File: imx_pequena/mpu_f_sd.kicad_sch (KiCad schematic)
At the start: 13 parts, among them J2 Micro_SD_Card, U1 MCIMX6Z0DVM09AB

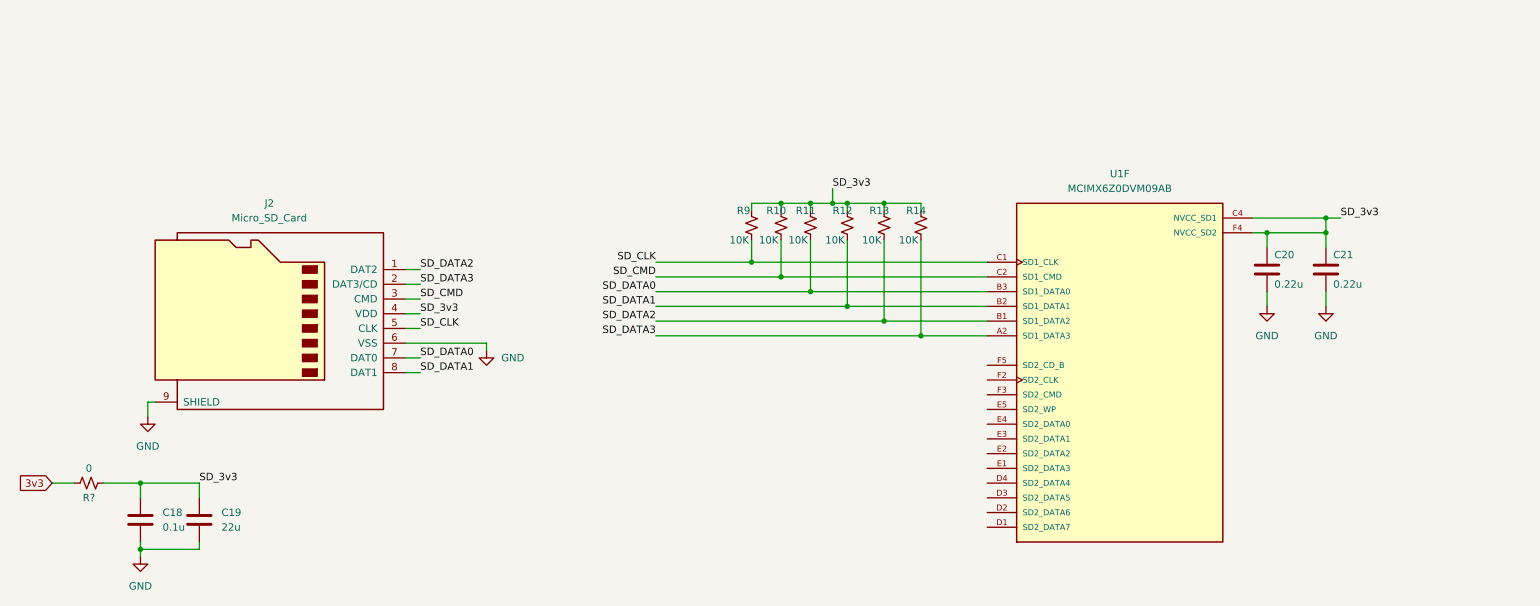
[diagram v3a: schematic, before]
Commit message: Updated pin mappings
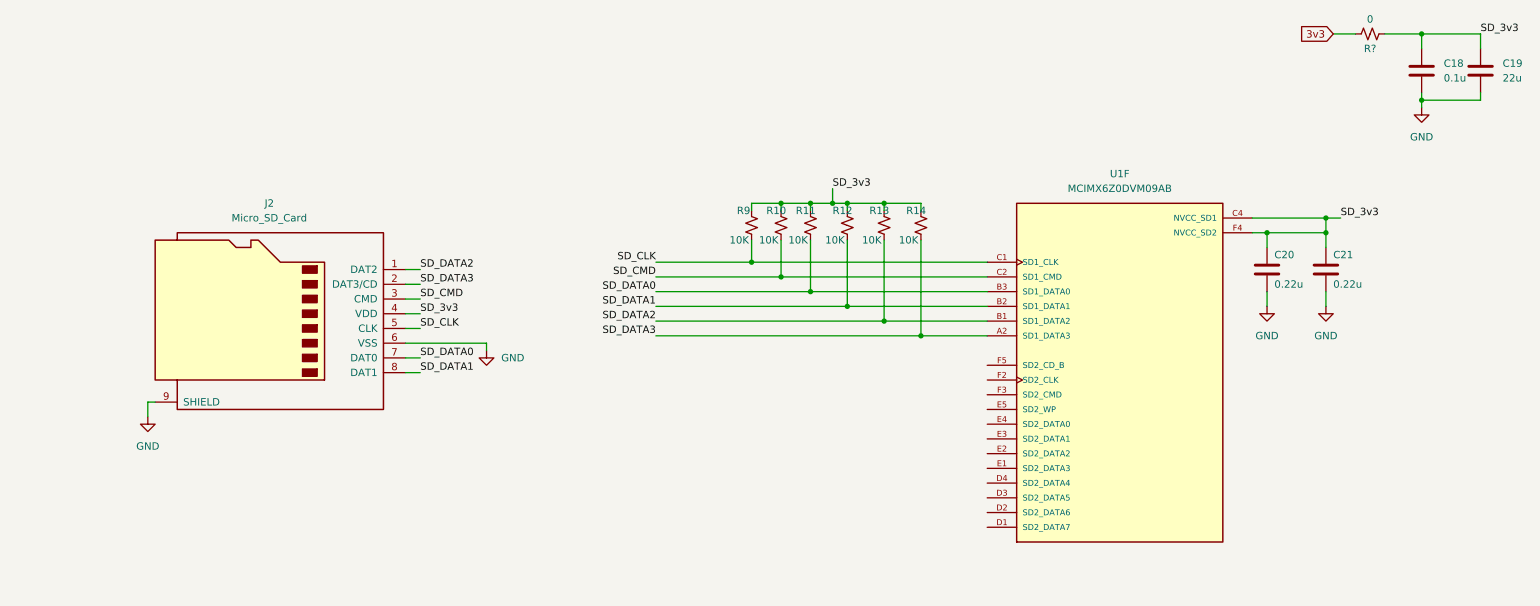
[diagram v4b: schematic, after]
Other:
- moved on the sheet: C18, C19, R?
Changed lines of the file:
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@@
   (junction (at 151.13 50.8) (diameter 0) (color 0 0 0 0)
   )
-  (junction (at 40.64 99.06) (diameter 0) (color 0 0 0 0)
+  (junction (at 261.62 21.59) (diameter 0) (color 0 0 0 0)
   )
   (junction (at 146.05 60.96) (diameter 0) (color 0 0 0 0)
@@
   (junction (at 156.21 50.8) (diameter 0) (color 0 0 0 0)
   )
-  (junction (at 40.64 110.49) (diameter 0) (color 0 0 0 0)
+  (junction (at 261.62 33.02) (diameter 0) (color 0 0 0 0)
   )
   (junction (at 160.02 50.8) (diameter 0) (color 0 0 0 0)
@@
     (stroke (width 0) (type default) (color 0 0 0 0))
   )
-  (wire (pts (xy 40.64 110.49) (xy 50.8 110.49))
+  (wire (pts (xy 261.62 33.02) (xy 271.78 33.02))
     (stroke (width 0) (type default) (color 0 0 0 0))
   )
@@
     (stroke (width 0) (type default) (color 0 0 0 0))
   )
-  (wire (pts (xy 40.64 109.22) (xy 40.64 110.49))
+  (wire (pts (xy 261.62 31.75) (xy 261.62 33.02))
     (stroke (width 0) (type default) (color 0 0 0 0))
   )
@@
     (stroke (width 0) (type default) (color 0 0 0 0))
   )
-  (wire (pts (xy 34.29 99.06) (xy 40.64 99.06))
+  (wire (pts (xy 255.27 21.59) (xy 261.62 21.59))
     (stroke (width 0) (type default) (color 0 0 0 0))
   )
@@
     (stroke (width 0) (type default) (color 0 0 0 0))
   )
-  (wire (pts (xy 50.8 99.06) (xy 50.8 101.6))
+  (wire (pts (xy 271.78 21.59) (xy 271.78 24.13))
     (stroke (width 0) (type default) (color 0 0 0 0))
   )
@@
     (stroke (width 0) (type default) (color 0 0 0 0))
   )
-  (wire (pts (xy 40.64 110.49) (xy 40.64 111.76))
+  (wire (pts (xy 261.62 33.02) (xy 261.62 34.29))
     (stroke (width 0) (type default) (color 0 0 0 0))
   )
@@
     (stroke (width 0) (type default) (color 0 0 0 0))
   )
-  (wire (pts (xy 50.8 110.49) (xy 50.8 109.22))
+  (wire (pts (xy 271.78 33.02) (xy 271.78 31.75))
     (stroke (width 0) (type default) (color 0 0 0 0))
   )
@@
     (stroke (width 0) (type default) (color 0 0 0 0))
   )
-  (wire (pts (xy 40.64 99.06) (xy 50.8 99.06))
+  (wire (pts (xy 261.62 21.59) (xy 271.78 21.59))
     (stroke (width 0) (type default) (color 0 0 0 0))
   )
@@
     (stroke (width 0) (type default) (color 0 0 0 0))
   )
-  (wire (pts (xy 29.21 99.06) (xy 25.4 99.06))
+  (wire (pts (xy 250.19 21.59) (xy 246.38 21.59))
     (stroke (width 0) (type default) (color 0 0 0 0))
   )
@@
     (stroke (width 0) (type default) (color 0 0 0 0))
   )
-  (wire (pts (xy 40.64 99.06) (xy 40.64 101.6))
+  (wire (pts (xy 261.62 21.59) (xy 261.62 24.13))
     (stroke (width 0) (type default) (color 0 0 0 0))
   )
@@
     (effects (font (size 1.27 1.27)) (justify left bottom))
   )
-  (label "SD_3v3" (at 50.8 99.06 0)
+  (label "SD_3v3" (at 271.78 21.59 0)
     (effects (font (size 1.27 1.27)) (justify left bottom))
   )
@@
     (effects (font (size 1.27 1.27)) (justify left bottom))
   )
-  (global_label "3v3" (shape input) (at 25.4 99.06 180) (fields_autoplaced)
+  (global_label "3v3" (shape input) (at 246.38 21.59 180) (fields_autoplaced)
     (effects (font (size 1.27 1.27)) (justify right))
-    (property "Intersheet References" "${INTERSHEET_REFS}" (id 0) (at 19.6002 99.1394 0)
+    (property "Intersheet References" "${INTERSHEET_REFS}" (id 0) (at 240.5802 21.6694 0)
       (effects (font (size 1.27 1.27)) (justify right) hide)
     )
@@
     (pin "1")
   )
-  (symbol (lib_id "Device:C") (at 50.8 105.41 0) (unit 1)
-    (in_bom yes) (on_board yes) (fields_autoplaced)
-    (property "Reference" "C19" (id 0) (at 54.61 104.1399 0)
-      (effects (font (size 1.27 1.27)) (justify left))
-    )
-    (property "Value" "22u" (id 1) (at 54.61 106.6799 0)
-      (effects (font (size 1.27 1.27)) (justify left))
-    )
-    (property "Footprint" "" (id 2) (at 51.7652 109.22 0)
-      (effects (font (size 1.27 1.27)) hide)
-    )
-    (property "Datasheet" "~" (id 3) (at 50.8 105.41 0)
+  (symbol (lib_id "Device:C") (at 271.78 27.94 0) (unit 1)
+    (in_bom yes) (on_board yes) (fields_autoplaced)
+    (property "Reference" "C19" (id 0) (at 275.59 26.6699 0)
+      (effects (font (size 1.27 1.27)) (justify left))
+    )
+    (property "Value" "22u" (id 1) (at 275.59 29.2099 0)
+      (effects (font (size 1.27 1.27)) (justify left))
+    )
+    (property "Footprint" "" (id 2) (at 272.7452 31.75 0)
+      (effects (font (size 1.27 1.27)) hide)
+    )
+    (property "Datasheet" "~" (id 3) (at 271.78 27.94 0)
       (effects (font (size 1.27 1.27)) hide)
     )
@@
     (pin "1")
   )
-  (symbol (lib_id "power:GND") (at 40.64 111.76 0) (unit 1)
-    (in_bom yes) (on_board yes) (fields_autoplaced)
-    (property "Reference" "#PWR0117" (id 0) (at 40.64 118.11 0)
-      (effects (font (size 1.27 1.27)) hide)
-    )
-    (property "Value" "GND" (id 1) (at 40.64 116.84 0))
-    (property "Footprint" "" (id 2) (at 40.64 111.76 0)
-      (effects (font (size 1.27 1.27)) hide)
-    )
-    (property "Datasheet" "" (id 3) (at 40.64 111.76 0)
+  (symbol (lib_id "power:GND") (at 261.62 34.29 0) (unit 1)
+    (in_bom yes) (on_board yes) (fields_autoplaced)
+    (property "Reference" "#PWR0117" (id 0) (at 261.62 40.64 0)
+      (effects (font (size 1.27 1.27)) hide)
+    )
+    (property "Value" "GND" (id 1) (at 261.62 39.37 0))
+    (property "Footprint" "" (id 2) (at 261.62 34.29 0)
+      (effects (font (size 1.27 1.27)) hide)
+    )
+    (property "Datasheet" "" (id 3) (at 261.62 34.29 0)
       (effects (font (size 1.27 1.27)) hide)
     )
@@
     (pin "1")
   )
-  (symbol (lib_id "Device:C") (at 40.64 105.41 0) (unit 1)
-    (in_bom yes) (on_board yes) (fields_autoplaced)
-    (property "Reference" "C18" (id 0) (at 44.45 104.1399 0)
-      (effects (font (size 1.27 1.27)) (justify left))
-    )
-    (property "Value" "0.1u" (id 1) (at 44.45 106.6799 0)
-      (effects (font (size 1.27 1.27)) (justify left))
-    )
-    (property "Footprint" "" (id 2) (at 41.6052 109.22 0)
-      (effects (font (size 1.27 1.27)) hide)
-    )
-    (property "Datasheet" "~" (id 3) (at 40.64 105.41 0)
+  (symbol (lib_id "Device:C") (at 261.62 27.94 0) (unit 1)
+    (in_bom yes) (on_board yes) (fields_autoplaced)
+    (property "Reference" "C18" (id 0) (at 265.43 26.6699 0)
+      (effects (font (size 1.27 1.27)) (justify left))
+    )
+    (property "Value" "0.1u" (id 1) (at 265.43 29.2099 0)
+      (effects (font (size 1.27 1.27)) (justify left))
+    )
+    (property "Footprint" "" (id 2) (at 262.5852 31.75 0)
+      (effects (font (size 1.27 1.27)) hide)
+    )
+    (property "Datasheet" "~" (id 3) (at 261.62 27.94 0)
       (effects (font (size 1.27 1.27)) hide)
     )
@@
     (pin "1")
   )
-  (symbol (lib_id "Device:R_Small_US") (at 31.75 99.06 270) (unit 1)
+  (symbol (lib_id "Device:R_Small_US") (at 252.73 21.59 270) (unit 1)
     (in_bom yes) (on_board yes)
-    (property "Reference" "R?" (id 0) (at 31.75 101.6 90))
-    (property "Value" "0" (id 1) (at 31.75 96.52 90))
-    (property "Footprint" "" (id 2) (at 31.75 99.06 0)
-      (effects (font (size 1.27 1.27)) hide)
-    )
-    (property "Datasheet" "~" (id 3) (at 31.75 99.06 0)
-      (effects (font (size 1.27 1.27)) hide)
-    )
+    (property "Reference" "R?" (id 0) (at 252.73 24.13 90))
+    (property "Value" "0" (id 1) (at 252.73 19.05 90))
+    (property "Footprint" "" (id 2) (at 252.73 21.59 0)
+      (effects (font (size 1.27 1.27)) hide)
+    )
+    (property "Datasheet" "~" (id 3) (at 252.73 21.59 0)
+      (effects (font (size 1.27 1.27)) hide)
+    )

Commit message: Part Assignment
Assigned GPIOs and assigned footprints to most parts
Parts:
- C18, C20, C21: footprint (none) -> Capacitor_SMD:C_0402_1005Metric
- C19: footprint (none) -> Capacitor_SMD:C_0805_2012Metric
- J2: footprint (none) -> Connector_Card:microSD_HC_Hirose_DM3AT-SF-PEJM5
- R10, R11, R12, R13, R14, R9: footprint (none) -> Resistor_SMD:R_0402_1005Metric
- R41: renamed from R?; footprint (none) -> Resistor_SMD:R_0402_1005Metric
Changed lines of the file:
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@@
       (effects (font (size 1.27 1.27)) (justify left))
     )
-    (property "Footprint" "" (id 2) (at 246.0752 66.04 0)
+    (property "Footprint" "Capacitor_SMD:C_0402_1005Metric" (id 2) (at 246.0752 66.04 0)
       (effects (font (size 1.27 1.27)) hide)
     )
@@
       (effects (font (size 1.27 1.27)) (justify left))
     )
-    (property "Footprint" "" (id 2) (at 156.21 54.61 0)
+    (property "Footprint" "Resistor_SMD:R_0402_1005Metric" (id 2) (at 156.21 54.61 0)
       (effects (font (size 1.27 1.27)) hide)
     )
@@
       (effects (font (size 1.27 1.27)) (justify left))
     )
-    (property "Footprint" "" (id 2) (at 146.05 54.61 0)
+    (property "Footprint" "Resistor_SMD:R_0402_1005Metric" (id 2) (at 146.05 54.61 0)
       (effects (font (size 1.27 1.27)) hide)
     )
@@
       (effects (font (size 1.27 1.27)) (justify left))
     )
-    (property "Footprint" "" (id 2) (at 175.26 54.61 0)
+    (property "Footprint" "Resistor_SMD:R_0402_1005Metric" (id 2) (at 175.26 54.61 0)
       (effects (font (size 1.27 1.27)) hide)
     )
@@
       (effects (font (size 1.27 1.27)) (justify left))
     )
-    (property "Footprint" "" (id 2) (at 272.7452 31.75 0)
+    (property "Footprint" "Capacitor_SMD:C_0805_2012Metric" (id 2) (at 272.7452 31.75 0)
       (effects (font (size 1.27 1.27)) hide)
     )
@@
       (effects (font (size 1.27 1.27)) (justify left))
     )
-    (property "Footprint" "" (id 2) (at 235.9152 66.04 0)
+    (property "Footprint" "Capacitor_SMD:C_0402_1005Metric" (id 2) (at 235.9152 66.04 0)
       (effects (font (size 1.27 1.27)) hide)
     )
@@
     (property "Reference" "J2" (id 0) (at 62.865 50.8 0))
     (property "Value" "Micro_SD_Card" (id 1) (at 62.865 53.34 0))
-    (property "Footprint" "" (id 2) (at 34.29 62.23 0)
+    (property "Footprint" "Connector_Card:microSD_HC_Hirose_DM3AT-SF-PEJM5" (id 2) (at 34.29 62.23 0)
       (effects (font (size 1.27 1.27)) hide)
     )
@@
       (effects (font (size 1.27 1.27)) (justify left))
     )
-    (property "Footprint" "" (id 2) (at 262.5852 31.75 0)
+    (property "Footprint" "Capacitor_SMD:C_0402_1005Metric" (id 2) (at 262.5852 31.75 0)
       (effects (font (size 1.27 1.27)) hide)
     )
@@
   (symbol (lib_id "Device:R_Small_US") (at 252.73 21.59 270) (unit 1)
     (in_bom yes) (on_board yes)
-    (property "Reference" "R?" (id 0) (at 252.73 24.13 90))
+    (property "Reference" "R41" (id 0) (at 252.73 24.13 90))
     (property "Value" "0" (id 1) (at 252.73 19.05 90))
-    (property "Footprint" "" (id 2) (at 252.73 21.59 0)
+    (property "Footprint" "Resistor_SMD:R_0402_1005Metric" (id 2) (at 252.73 21.59 0)
       (effects (font (size 1.27 1.27)) hide)
     )
@@
       (effects (font (size 1.27 1.27)) (justify left))
     )
-    (property "Footprint" "" (id 2) (at 168.91 54.61 0)
+    (property "Footprint" "Resistor_SMD:R_0402_1005Metric" (id 2) (at 168.91 54.61 0)
       (effects (font (size 1.27 1.27)) hide)
     )
@@
       (effects (font (size 1.27 1.27)) (justify left))
     )
-    (property "Footprint" "" (id 2) (at 162.56 54.61 0)
+    (property "Footprint" "Resistor_SMD:R_0402_1005Metric" (id 2) (at 162.56 54.61 0)
       (effects (font (size 1.27 1.27)) hide)
     )
@@
       (effects (font (size 1.27 1.27)) (justify left))
     )
-    (property "Footprint" "" (id 2) (at 151.13 54.61 0)
-      (effects (font (size 1.27 1.27)) hide)
-    )
+    (property "Footprint" "Resistor_SMD:R_0402_1005Metric" (id 2) (at 151.13 54.61 0)
+      (effects (font (size 1.27 1.27)) hide)
+    )

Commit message: lots of updates
Set design rules, fixed ERC, etc....
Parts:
- J2: footprint Connector_Card:microSD_HC_Hirose_DM3AT-SF-PEJM5 -> (none)
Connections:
- no-connect marks 0 -> 12
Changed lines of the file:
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@@
   (junction (at 156.21 66.04) (diameter 0) (color 0 0 0 0)
   )
+  (no_connect (at 177.8 88.9))
+  (no_connect (at 177.8 78.74))
+  (no_connect (at 177.8 99.06))
+  (no_connect (at 177.8 83.82))
+  (no_connect (at 177.8 104.14))
+  (no_connect (at 177.8 101.6))
+  (no_connect (at 177.8 96.52))
+  (no_connect (at 177.8 81.28))
+  (no_connect (at 177.8 91.44))
+  (no_connect (at 177.8 106.68))
+  (no_connect (at 177.8 86.36))
+  (no_connect (at 177.8 93.98))
   (wire (pts (xy 151.13 63.5) (xy 186.69 63.5))
     (stroke (width 0) (type default) (color 0 0 0 0))
@@
     (stroke (width 0) (type default) (color 0 0 0 0))
   )
+  (wire (pts (xy 177.8 88.9) (xy 186.69 88.9))
+    (stroke (width 0) (type default) (color 0 0 0 0))
+  )
   (wire (pts (xy 129.54 63.5) (xy 151.13 63.5))
     (stroke (width 0) (type default) (color 0 0 0 0))
   )
+  (wire (pts (xy 177.8 93.98) (xy 186.69 93.98))
+    (stroke (width 0) (type default) (color 0 0 0 0))
+  )
   (wire (pts (xy 86.36 74.93) (xy 100.33 74.93))
     (stroke (width 0) (type default) (color 0 0 0 0))
@@
     (stroke (width 0) (type default) (color 0 0 0 0))
   )
+  (wire (pts (xy 177.8 81.28) (xy 186.69 81.28))
+    (stroke (width 0) (type default) (color 0 0 0 0))
+  )
+  (wire (pts (xy 177.8 106.68) (xy 186.69 106.68))
+    (stroke (width 0) (type default) (color 0 0 0 0))
+  )
   (wire (pts (xy 151.13 57.15) (xy 151.13 63.5))
     (stroke (width 0) (type default) (color 0 0 0 0))
   )
+  (wire (pts (xy 177.8 86.36) (xy 186.69 86.36))
+    (stroke (width 0) (type default) (color 0 0 0 0))
+  )
   (wire (pts (xy 175.26 57.15) (xy 175.26 73.66))
     (stroke (width 0) (type default) (color 0 0 0 0))
@@
     (stroke (width 0) (type default) (color 0 0 0 0))
   )
+  (wire (pts (xy 177.8 101.6) (xy 186.69 101.6))
+    (stroke (width 0) (type default) (color 0 0 0 0))
+  )
   (wire (pts (xy 271.78 21.59) (xy 271.78 24.13))
     (stroke (width 0) (type default) (color 0 0 0 0))
@@
     (stroke (width 0) (type default) (color 0 0 0 0))
   )
+  (wire (pts (xy 177.8 78.74) (xy 186.69 78.74))
+    (stroke (width 0) (type default) (color 0 0 0 0))
+  )
   (wire (pts (xy 41.91 85.09) (xy 43.18 85.09))
     (stroke (width 0) (type default) (color 0 0 0 0))
@@
     (stroke (width 0) (type default) (color 0 0 0 0))
   )
+  (wire (pts (xy 177.8 91.44) (xy 186.69 91.44))
+    (stroke (width 0) (type default) (color 0 0 0 0))
+  )
   (wire (pts (xy 245.11 58.42) (xy 245.11 55.88))
     (stroke (width 0) (type default) (color 0 0 0 0))
@@
     (stroke (width 0) (type default) (color 0 0 0 0))
   )
+  (wire (pts (xy 177.8 99.06) (xy 186.69 99.06))
+    (stroke (width 0) (type default) (color 0 0 0 0))
+  )
   (wire (pts (xy 129.54 73.66) (xy 175.26 73.66))
     (stroke (width 0) (type default) (color 0 0 0 0))
@@
     (stroke (width 0) (type default) (color 0 0 0 0))
   )
+  (wire (pts (xy 177.8 96.52) (xy 186.69 96.52))
+    (stroke (width 0) (type default) (color 0 0 0 0))
+  )
   (wire (pts (xy 261.62 21.59) (xy 261.62 24.13))
     (stroke (width 0) (type default) (color 0 0 0 0))
@@
     (stroke (width 0) (type default) (color 0 0 0 0))
   )
+  (wire (pts (xy 177.8 104.14) (xy 186.69 104.14))
+    (stroke (width 0) (type default) (color 0 0 0 0))
+  )
   (wire (pts (xy 175.26 50.8) (xy 175.26 52.07))
     (stroke (width 0) (type default) (color 0 0 0 0))
   )
   (wire (pts (xy 162.56 68.58) (xy 186.69 68.58))
+    (stroke (width 0) (type default) (color 0 0 0 0))
+  )
+  (wire (pts (xy 177.8 83.82) (xy 186.69 83.82))
     (stroke (width 0) (type default) (color 0 0 0 0))
   )
@@
     (property "Reference" "J2" (id 0) (at 62.865 50.8 0))
     (property "Value" "Micro_SD_Card" (id 1) (at 62.865 53.34 0))
-    (property "Footprint" "Connector_Card:microSD_HC_Hirose_DM3AT-SF-PEJM5" (id 2) (at 34.29 62.23 0)
-      (effects (font (size 1.27 1.27)) hide)
-    )
+    (property "Footprint" "" (id 2) (at 34.29 62.23 0)
+      (effects (font (size 1.27 1.27)) hide)
+    )

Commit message: fixed part alllocation
fixed socket to pin header issue
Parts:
- J2: footprint (none) -> Connector_Card:microSD_HC_Hirose_DM3AT-SF-PEJM5
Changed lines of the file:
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@@
     (property "Reference" "J2" (id 0) (at 62.865 50.8 0))
     (property "Value" "Micro_SD_Card" (id 1) (at 62.865 53.34 0))
-    (property "Footprint" "" (id 2) (at 34.29 62.23 0)
+    (property "Footprint" "Connector_Card:microSD_HC_Hirose_DM3AT-SF-PEJM5" (id 2) (at 34.29 62.23 0)
       (effects (font (size 1.27 1.27)) hide)
     )
